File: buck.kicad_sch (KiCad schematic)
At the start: 65 parts, among them Q4 AO3400A, Q5 AO3400A, U14 SL78L05, U17 MIC4605-2YM-TR, U20 AD8038, U21 MCP6571T-E/OT

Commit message: pcb layout draft
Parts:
- C10, C14, C15, C17, C18, C19, C20, C21, C22, C26, C27, C28, C29, C30, C31, C32, C33, C34, C35, C36, C37, C38, C39, C40, C48, C49: footprint Capacitor_SMD:C_0805_2012Metric -> footprints_pretty:0805_cap_nosilk
- R26, R27, R28, R29, R30, R31, R32, R33, R46, R47, R48, R50, R51, R52, R53, R54, R67, Re1, Re2, Re3, Re4: footprint Resistor_SMD:R_0805_2012Metric -> footprints_pretty:res_0805_nosilk
- TP13: footprint TestPoint:TestPoint_Plated_Hole_D2.0mm -> TestPoint:TestPoint_Pad_D1.0mm
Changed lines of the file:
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@@
 			)
 		)
-		(property "Footprint" "Capacitor_SMD:C_0805_2012Metric"
+		(property "Footprint" "footprints_pretty:0805_cap_nosilk"
 			(at 152.7048 80.645 0)
 			(effects
@@
 			)
 		)
-		(property "Footprint" "Capacitor_SMD:C_0805_2012Metric"
+		(property "Footprint" "footprints_pretty:0805_cap_nosilk"
 			(at 226.9998 66.04 0)
 			(effects
@@
 			)
 		)
-		(property "Footprint" "Resistor_SMD:R_0805_2012Metric"
+		(property "Footprint" "footprints_pretty:res_0805_nosilk"
 			(at 244.602 73.025 90)
 			(effects
@@
 			)
 		)
-		(property "Footprint" "Resistor_SMD:R_0805_2012Metric"
+		(property "Footprint" "footprints_pretty:res_0805_nosilk"
 			(at 33.147 98.425 90)
 			(effects
@@
 			)
 		)
-		(property "Footprint" "Resistor_SMD:R_0805_2012Metric"
+		(property "Footprint" "footprints_pretty:res_0805_nosilk"
 			(at 261.112 142.24 90)
 			(effects
@@
 			)
 		)
-		(property "Footprint" "Capacitor_SMD:C_0805_2012Metric"
+		(property "Footprint" "footprints_pretty:0805_cap_nosilk"
 			(at 240.03 81.6102 0)
 			(effects
@@
 			)
 		)
-		(property "Footprint" "Capacitor_SMD:C_0805_2012Metric"
+		(property "Footprint" "footprints_pretty:0805_cap_nosilk"
 			(at 240.03 96.8502 0)
 			(effects
@@
 			)
 		)
-		(property "Footprint" "Capacitor_SMD:C_0805_2012Metric"
+		(property "Footprint" "footprints_pretty:0805_cap_nosilk"
 			(at 135.5598 80.645 0)
 			(effects
@@
 			)
 		)
-		(property "Footprint" "Capacitor_SMD:C_0805_2012Metric"
+		(property "Footprint" "footprints_pretty:0805_cap_nosilk"
 			(at 234.95 108.2802 0)
 			(effects
@@
 			)
 		)
-		(property "Footprint" "Resistor_SMD:R_0805_2012Metric"
+		(property "Footprint" "footprints_pretty:res_0805_nosilk"
 			(at 231.902 73.025 90)
 			(effects
@@
 			)
 		)
-		(property "Footprint" "Resistor_SMD:R_0805_2012Metric"
+		(property "Footprint" "footprints_pretty:res_0805_nosilk"
 			(at 241.3 130.048 90)
 			(effects
@@
 			)
 		)
-		(property "Footprint" "Resistor_SMD:R_0805_2012Metric"
+		(property "Footprint" "footprints_pretty:res_0805_nosilk"
 			(at 241.3 123.063 90)
 			(effects
@@
 			)
 		)
-		(property "Footprint" "Capacitor_SMD:C_0805_2012Metric"
+		(property "Footprint" "footprints_pretty:0805_cap_nosilk"
 			(at 234.95 128.6002 0)
 			(effects
@@
 			)
 		)
-		(property "Footprint" "Resistor_SMD:R_0805_2012Metric"
+		(property "Footprint" "footprints_pretty:res_0805_nosilk"
 			(at 264.287 142.24 90)
 			(effects
@@
 			)
 		)
-		(property "Footprint" "Capacitor_SMD:C_0805_2012Metric"
+		(property "Footprint" "footprints_pretty:0805_cap_nosilk"
 			(at 234.95 123.5202 0)
 			(effects
@@
 			)
 		)
-		(property "Footprint" "Resistor_SMD:R_0805_2012Metric"
+		(property "Footprint" "footprints_pretty:res_0805_nosilk"
 			(at 270.637 65.405 90)
 			(effects
@@
 			)
 		)
-		(property "Footprint" "Capacitor_SMD:C_0805_2012Metric"
+		(property "Footprint" "footprints_pretty:0805_cap_nosilk"
 			(at 95.5802 46.99 0)
 			(effects
@@
 			)
 		)
-		(property "Footprint" "Capacitor_SMD:C_0805_2012Metric"
+		(property "Footprint" "footprints_pretty:0805_cap_nosilk"
 			(at 244.1448 66.04 0)
 			(effects
@@
 			)
 		)
-		(property "Footprint" "Resistor_SMD:R_0805_2012Metric"
+		(property "Footprint" "footprints_pretty:res_0805_nosilk"
 			(at 241.427 73.025 90)
 			(effects
@@
 			)
 		)
-		(property "Footprint" "Capacitor_SMD:C_0805_2012Metric"
+		(property "Footprint" "footprints_pretty:0805_cap_nosilk"
 			(at 240.03 91.7702 0)
 			(effects
@@
 			)
 		)
-		(property "Footprint" "Capacitor_SMD:C_0805_2012Metric"
+		(property "Footprint" "footprints_pretty:0805_cap_nosilk"
 			(at 158.4198 80.645 0)
 			(effects
@@
 			)
 		)
-		(property "Footprint" "Capacitor_SMD:C_0805_2012Metric"
+		(property "Footprint" "footprints_pretty:0805_cap_nosilk"
 			(at 79.0448 133.35 0)
 			(effects
@@
 			)
 		)
-		(property "Footprint" "Resistor_SMD:R_0805_2012Metric"
+		(property "Footprint" "footprints_pretty:res_0805_nosilk"
 			(at 274.447 65.405 90)
 			(effects
@@
 			)
 		)
-		(property "Footprint" "TestPoint:TestPoint_Plated_Hole_D2.0mm"
+		(property "Footprint" "TestPoint:TestPoint_Pad_D1.0mm"
 			(at 62.23 115.57 0)
 			(effects
@@
 			)
 		)
-		(property "Footprint" "Resistor_SMD:R_0805_2012Metric"
+		(property "Footprint" "footprints_pretty:res_0805_nosilk"
 			(at 241.3 126.238 90)
 			(effects
@@
 			)
 		)
-		(property "Footprint" "Capacitor_SMD:C_0805_2012Metric"
+		(property "Footprint" "footprints_pretty:0805_cap_nosilk"
 			(at 31.4198 92.71 0)
 			(effects
@@
 			)
 		)
-		(property "Footprint" "Capacitor_SMD:C_0805_2012Metric"
+		(property "Footprint" "footprints_pretty:0805_cap_nosilk"
 			(at 240.03 86.6902 0)
 			(effects
@@
 			)
 		)
-		(property "Footprint" "Capacitor_SMD:C_0805_2012Metric"
+		(property "Footprint" "footprints_pretty:0805_cap_nosilk"
 			(at 242.2398 156.21 0)
 			(effects
@@
 			)
 		)
-		(property "Footprint" "Resistor_SMD:R_0805_2012Metric"
+		(property "Footprint" "footprints_pretty:res_0805_nosilk"
 			(at 267.462 142.24 90)
 			(effects
@@
 			)
 		)
-		(property "Footprint" "Capacitor_SMD:C_0805_2012Metric"
+		(property "Footprint" "footprints_pretty:0805_cap_nosilk"
 			(at 238.4298 66.04 0)
 			(effects
@@
 			)
 		)
-		(property "Footprint" "Capacitor_SMD:C_0805_2012Metric"
+		(property "Footprint" "footprints_pretty:0805_cap_nosilk"
 			(at 249.8598 66.04 0)
 			(effects
@@
 			)
 		)
-		(property "Footprint" "Resistor_SMD:R_0805_2012Metric"
+		(property "Footprint" "footprints_pretty:res_0805_nosilk"
 			(at 241.3 116.713 90)
 			(effects
@@
 			)
 		)
-		(property "Footprint" "Capacitor_SMD:C_0805_2012Metric"
+		(property "Footprint" "footprints_pretty:0805_cap_nosilk"
 			(at 141.2748 80.645 0)
 			(effects
@@
 			)
 		)
-		(property "Footprint" "Capacitor_SMD:C_0805_2012Metric"
+		(property "Footprint" "footprints_pretty:0805_cap_nosilk"
 			(at 65.405 46.0248 0)
 			(effects
@@
 			)
 		)
-		(property "Footprint" "Resistor_SMD:R_0805_2012Metric"
+		(property "Footprint" "footprints_pretty:res_0805_nosilk"
 			(at 262.382 65.405 90)
 			(effects
@@
 			)
 		)
-		(property "Footprint" "Resistor_SMD:R_0805_2012Metric"
+		(property "Footprint" "footprints_pretty:res_0805_nosilk"
 			(at 249.682 73.025 90)
 			(effects
@@
 			)
 		)
-		(property "Footprint" "Capacitor_SMD:C_0805_2012Metric"
+		(property "Footprint" "footprints_pretty:0805_cap_nosilk"
 			(at 234.95 118.4402 0)
 			(effects
@@
 			)
 		)
-		(property "Footprint" "Resistor_SMD:R_0805_2012Metric"
+		(property "Footprint" "footprints_pretty:res_0805_nosilk"
 			(at 241.3 119.888 90)
 			(effects
@@
 			)
 		)
-		(property "Footprint" "Capacitor_SMD:C_0805_2012Metric"
+		(property "Footprint" "footprints_pretty:0805_cap_nosilk"
 			(at 41.6052 73.025 0)
 			(effects
@@
 			)
 		)
-		(property "Footprint" "Resistor_SMD:R_0805_2012Metric"
+		(property "Footprint" "footprints_pretty:res_0805_nosilk"
 			(at 257.937 65.405 90)
 			(effects
@@
 			)
 		)
-		(property "Footprint" "Capacitor_SMD:C_0805_2012Metric"
+		(property "Footprint" "footprints_pretty:0805_cap_nosilk"
 			(at 232.7148 66.04 0)
 			(effects
@@
 			)
 		)
-		(property "Footprint" "Capacitor_SMD:C_0805_2012Metric"
+		(property "Footprint" "footprints_pretty:0805_cap_nosilk"
 			(at 240.03 102.5652 0)
 			(effects
@@
 			)
 		)
-		(property "Footprint" "Resistor_SMD:R_0805_2012Metric"
+		(property "Footprint" "footprints_pretty:res_0805_nosilk"
 			(at 254.762 142.24 90)
 			(effects
@@
 			)
 		)
-		(property "Footprint" "Capacitor_SMD:C_0805_2012Metric"
+		(property "Footprint" "footprints_pretty:0805_cap_nosilk"
 			(at 234.95 113.3602 0)
 			(effects
@@
 			)
 		)
-		(property "Footprint" "Resistor_SMD:R_0805_2012Metric"
+		(property "Footprint" "footprints_pretty:res_0805_nosilk"
 			(at 257.937 142.24 90)
 			(effects
@@
 			)
 		)
-		(property "Footprint" "Resistor_SMD:R_0805_2012Metric"
+		(property "Footprint" "footprints_pretty:res_0805_nosilk"
 			(at 236.982 73.025 90)
 			(effects
@@
 			)
 		)
-		(property "Footprint" "Resistor_SMD:R_0805_2012Metric"
+		(property "Footprint" "footprints_pretty:res_0805_nosilk"
 			(at 266.827 65.405 90)
 			(effects
@@
 			)
 		)
-		(property "Footprint" "Capacitor_SMD:C_0805_2012Metric"
+		(property "Footprint" "footprints_pretty:0805_cap_nosilk"
 			(at 146.9898 80.645 0)
 			(effects

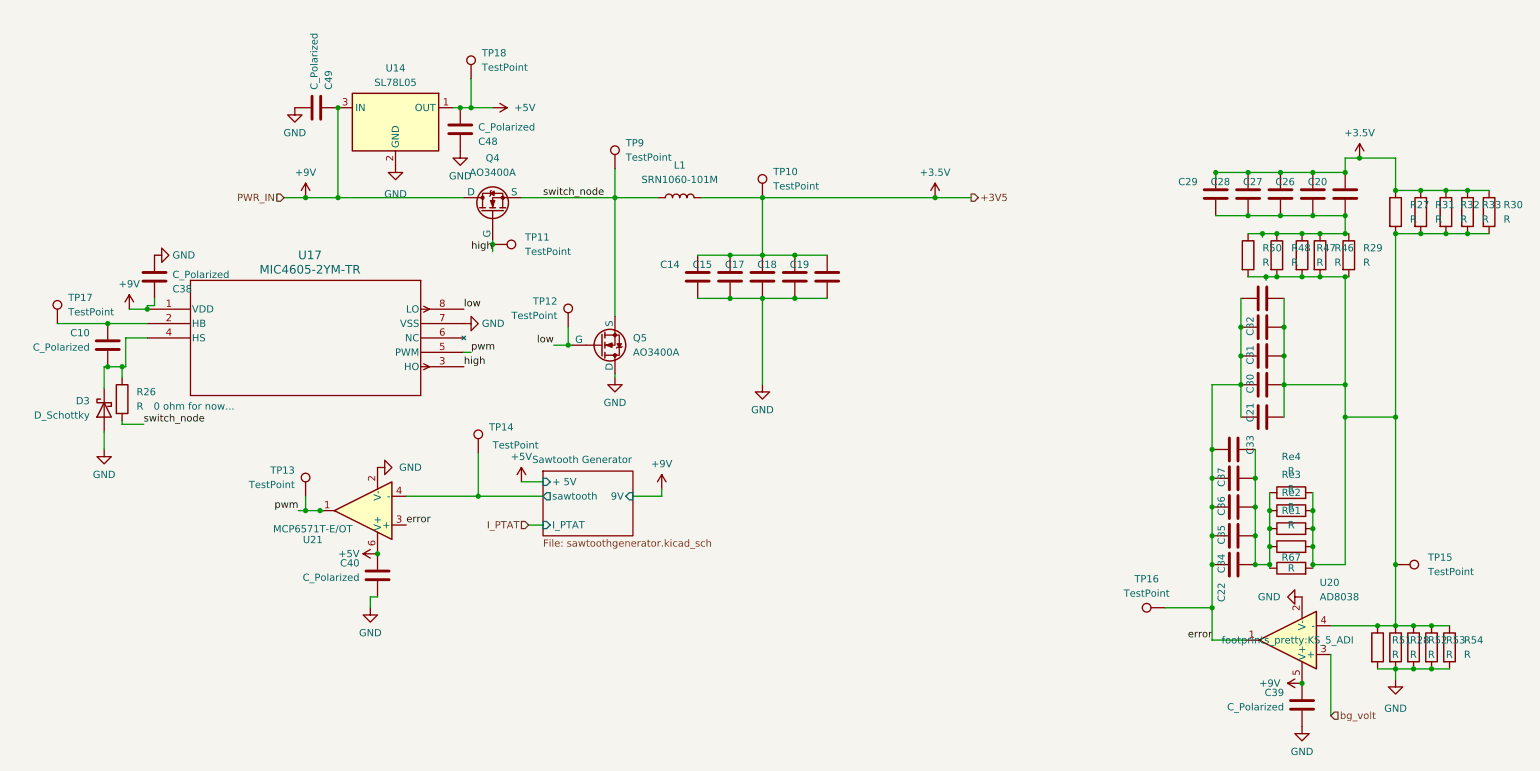
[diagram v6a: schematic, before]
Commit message: values added for buck
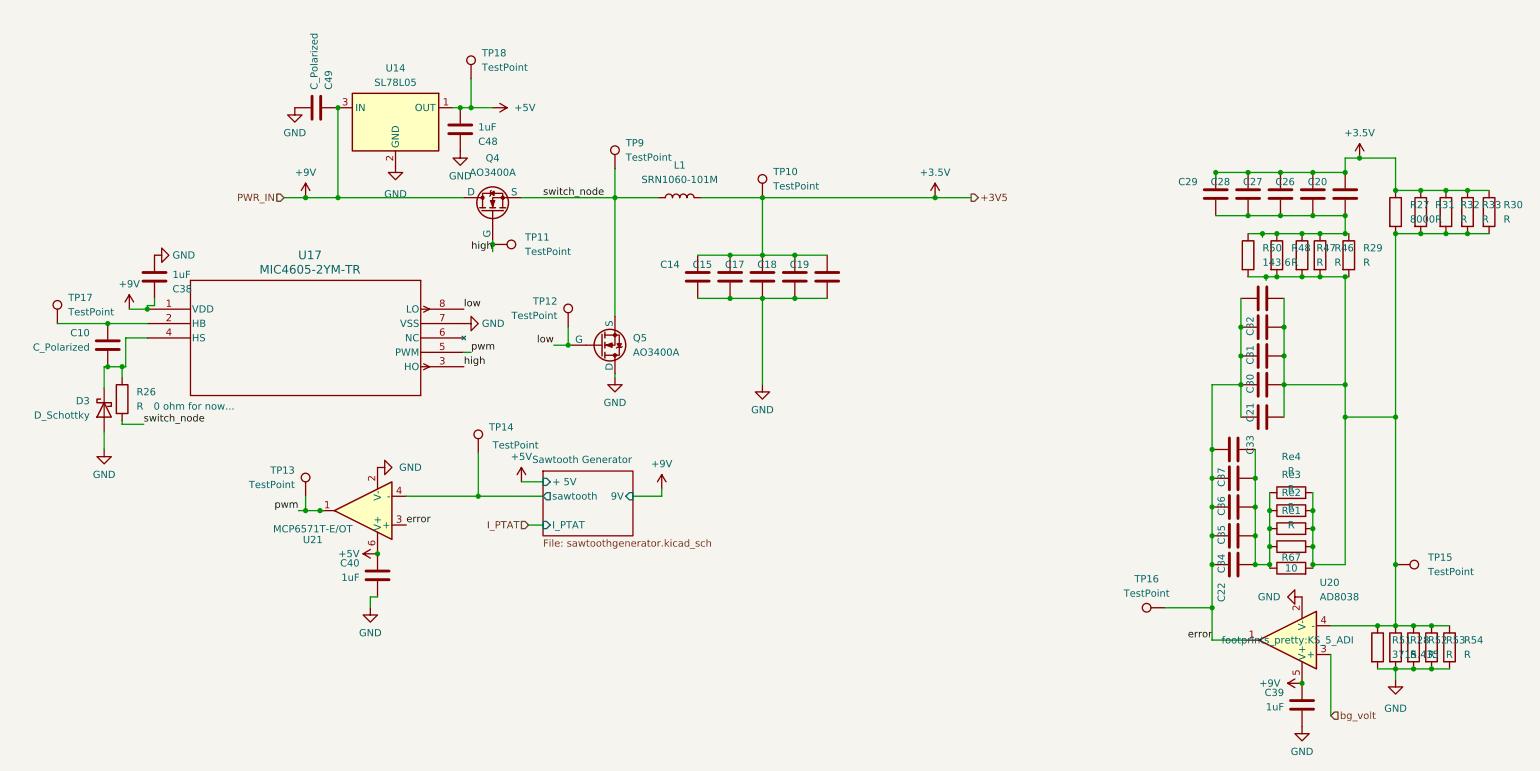
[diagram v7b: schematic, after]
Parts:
- C29: value C_Polarized -> 391nF
- C30: value C_Polarized -> 407nF
- C36: value C_Polarized -> 18uF
- C38, C39, C40, C48: value C_Polarized -> 1uF
- R27: value R -> 8000
- R50: value R -> 143.6
- R51: value R -> 3715.435
- R67: value R -> 10
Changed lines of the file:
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@@
 			)
 		)
-		(property "Value" "C_Polarized"
+		(property "Value" "391nF"
 			(at 224.79 62.6109 0)
 			(effects
@@
 			)
 		)
-		(property "Value" "R"
+		(property "Value" "143.6"
 			(at 236.22 74.2949 0)
 			(effects
@@
 			)
 		)
-		(property "Value" "R"
+		(property "Value" "10"
 			(at 241.3 128.27 90)
 			(effects
@@
 			)
 		)
-		(property "Value" "C_Polarized"
+		(property "Value" "1uF"
 			(at 97.79 50.4191 0)
 			(effects
@@
 			)
 		)
-		(property "Value" "C_Polarized"
+		(property "Value" "407nF"
 			(at 236.6009 93.98 0)
 			(effects
@@
 			)
 		)
-		(property "Value" "C_Polarized"
+		(property "Value" "1uF"
 			(at 76.835 129.9209 0)
 			(effects
@@
 			)
 		)
-		(property "Value" "C_Polarized"
+		(property "Value" "1uF"
 			(at 240.03 152.7809 0)
 			(effects
@@
 			)
 		)
-		(property "Value" "C_Polarized"
+		(property "Value" "1uF"
 			(at 43.815 76.4541 0)
 			(effects
@@
 			)
 		)
-		(property "Value" "R"
+		(property "Value" "8000"
 			(at 262.255 66.6749 0)
 			(effects
@@
 			)
 		)
-		(property "Value" "R"
+		(property "Value" "3715.435"
 			(at 259.08 143.5099 0)
 			(effects
@@
 			)
 		)
-		(property "Value" "C_Polarized"
+		(property "Value" "18uF"
 			(at 231.5209 115.57 0)
 			(effects
